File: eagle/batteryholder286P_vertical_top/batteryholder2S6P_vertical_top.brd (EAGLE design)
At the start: 84.5 x 34.5 mm, 3 parts, among them J2 5.5x2.1mm Barrel

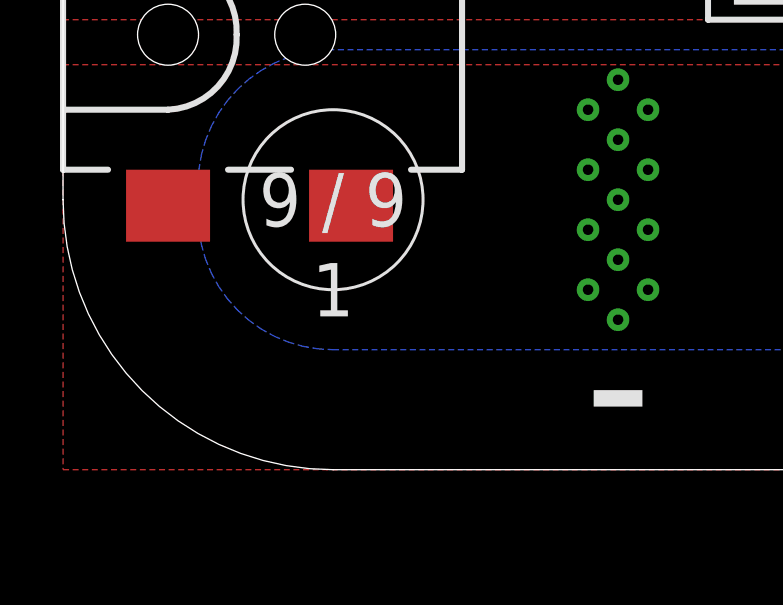
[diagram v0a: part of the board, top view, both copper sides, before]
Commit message: eagle: rename batteryholder vertical
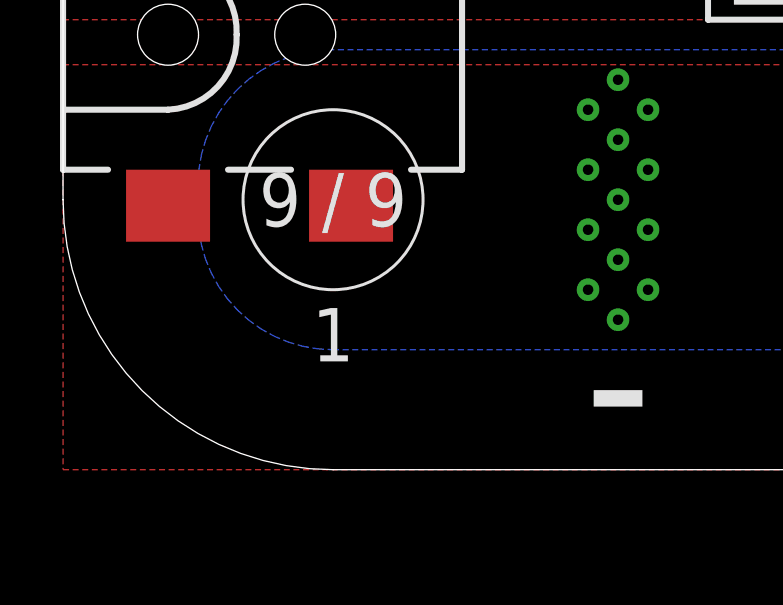
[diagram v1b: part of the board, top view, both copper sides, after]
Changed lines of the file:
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@@
 <text x="37.5" y="25.5" size="1.778" layer="25" align="center">37,5 / 25,5</text>
 <text x="18.5" y="25.5" size="1.778" layer="25" align="center">18,5 / 25,5</text>
-<text x="9" y="6" size="1.778" layer="21" align="center">1</text>
+<text x="9" y="4.5" size="1.778" layer="21" align="center">1</text>
 <text x="28" y="9" size="1.778" layer="21" align="center">3</text>
 <text x="47" y="9" size="1.778" layer="21" align="center">5</text>
